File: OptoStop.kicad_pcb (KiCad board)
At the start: 2 copper layers, 24.8 x 14 mm, 10 parts, among them IC1 OPTO-ENDSTOP, P1 CONN_01X03

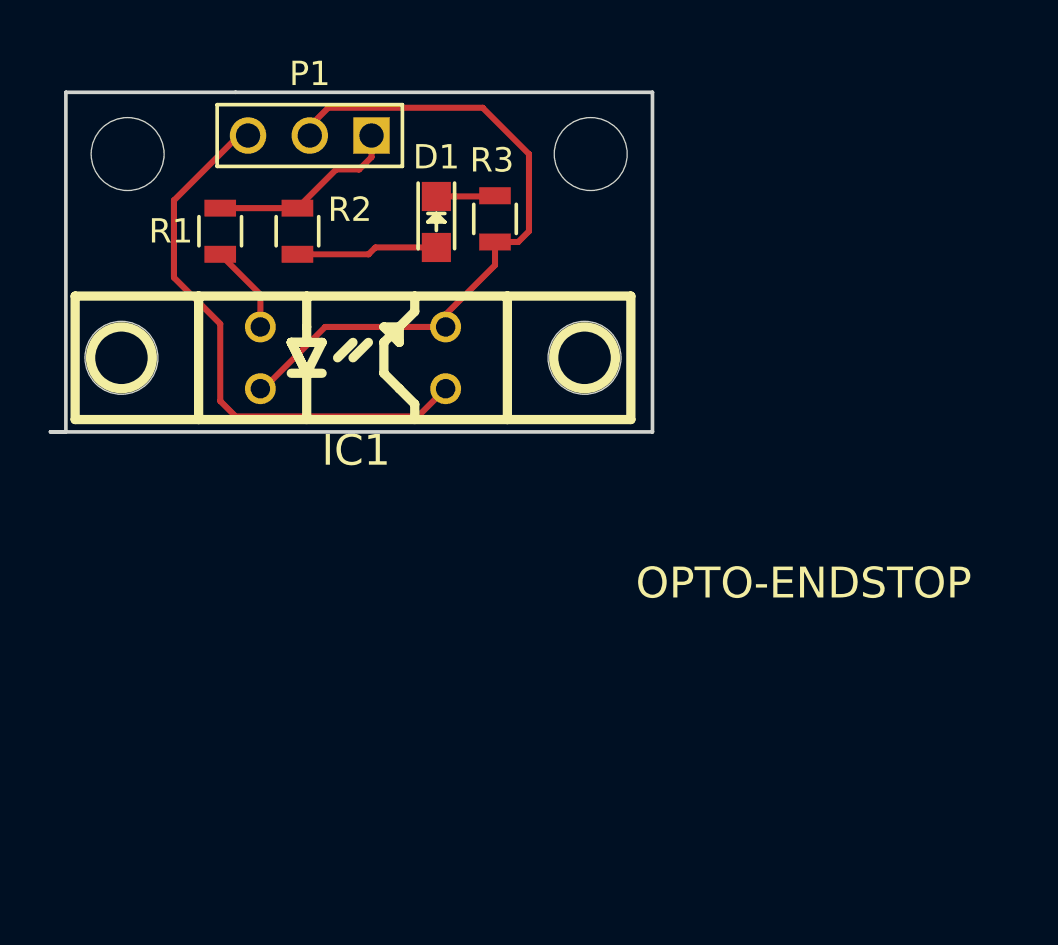
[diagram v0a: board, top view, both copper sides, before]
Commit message: thickened traces
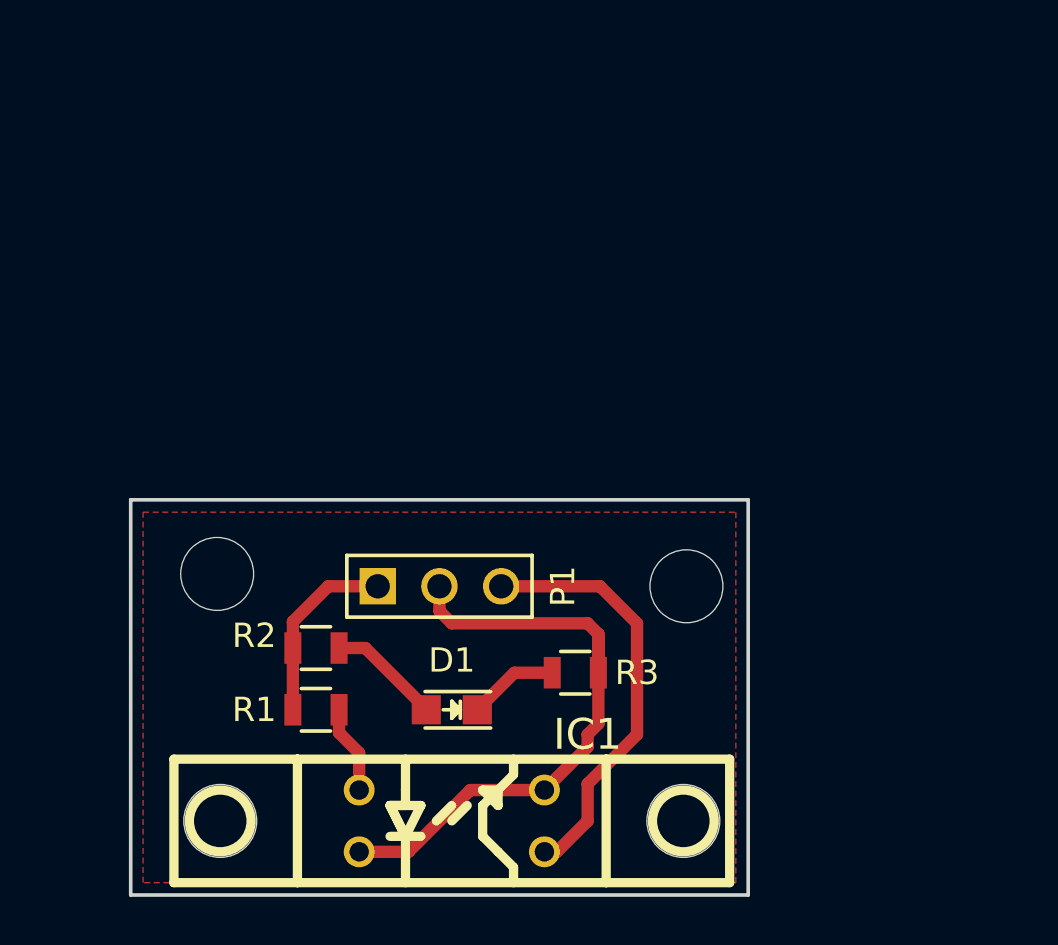
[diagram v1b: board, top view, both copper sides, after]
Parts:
- moved W3 29.1 mm to (159.5, 104.1)
- moved W4 23.1 mm to (140.2, 103.6)
- moved D1 20.1 mm to (149.9, 109.2), turned to 180 degrees
- moved R1 20.1 mm to (144.3, 109.2), turned to 0 degrees
- moved IC1 19.5 mm to (149.9, 113.8)
- moved W1 19.5 mm to (140.3, 113.8)
- moved W2 19.5 mm to (159.4, 113.8)
- moved P1 19.3 mm to (149.4, 104.1), turned to 0 degrees
- moved R3 19.0 mm to (154.9, 107.7), turned to 180 degrees
- moved R2 17.2 mm to (144.3, 106.7), turned to 0 degrees
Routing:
- net /Sig: track 23.2 -> 17.5 mm
- net /GND: track 28.0 -> 25.0 mm
- net Net-(D1-Pad1): track 2.42 -> 3.71 mm
- net Net-(D1-Pad2): track 5.83 -> 4.66 mm
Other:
- board size 24.8 x 14 mm -> 25.4 x 16.3 mm

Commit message: renders
made renders and some small updates
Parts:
- IC1, P1: moved to B.Cu
- moved R3 2.27 mm to (152.9, 108.7), turned to 90 degrees
- moved D1 1.37 mm to (149.4, 108.0)
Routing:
- net /Sig: track 17.5 -> 12.9 mm
- net Net-(IC1-PadA/+): track 3.64 -> 7.42 mm
- net Net-(D1-Pad2): track 4.66 -> 3.61 mm
- net /GND: track 25.0 -> 25.9 mm
- net Net-(D1-Pad1): track 3.71 -> 2.94 mm
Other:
- board text added: "LED"
